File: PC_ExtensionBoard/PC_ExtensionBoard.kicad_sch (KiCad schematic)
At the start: 0 parts

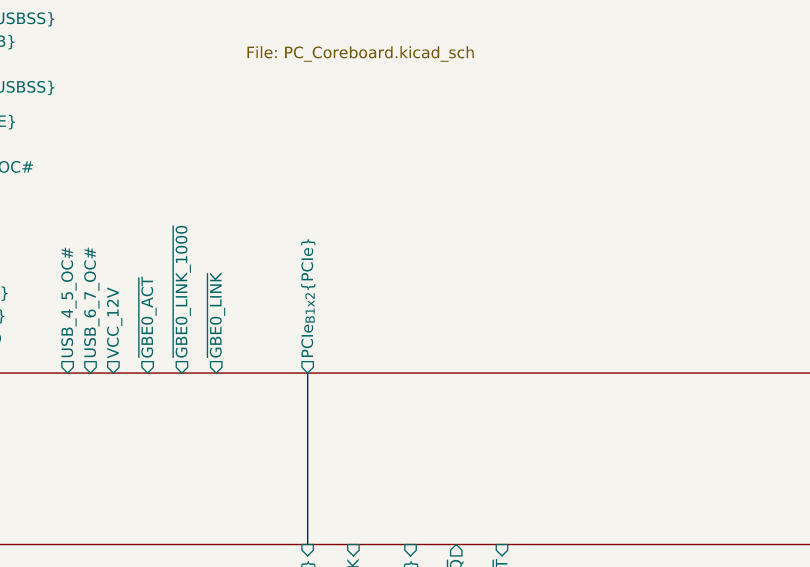
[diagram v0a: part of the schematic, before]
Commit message: update LCSC
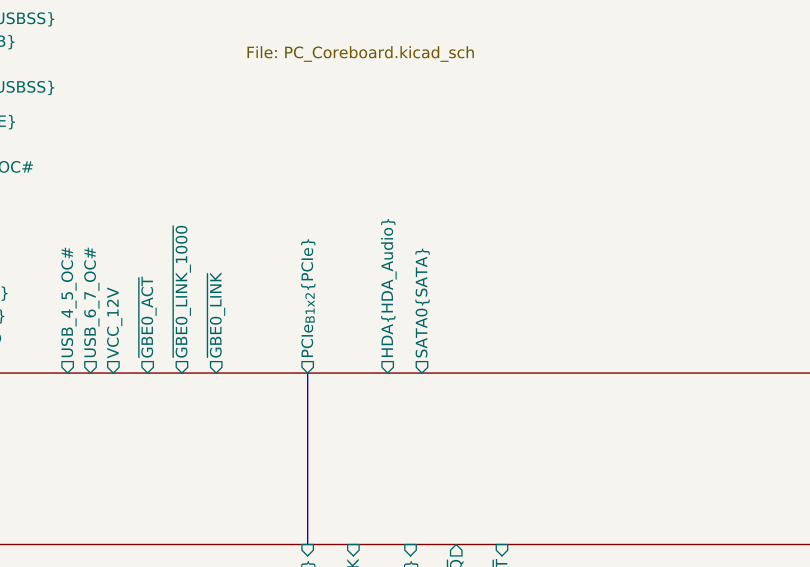
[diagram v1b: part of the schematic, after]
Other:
- sheet PC_CoreBoard ports: added HDA{HDA_Audio}, SATA0{SATA}; removed none
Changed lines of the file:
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@@
+			)
+		)
+		(pin "HDA{HDA_Audio}" output
+			(at 257.81 314.96 270)
+			(effects
+				(font
+					(size 1.27 1.27)
+				)
+				(justify left)
+			)
+		)
+		(pin "SATA0{SATA}" output
+			(at 261.62 314.96 270)
+			(effects
+				(font
+					(size 1.27 1.27)
+				)
+				(justify left)
 			)
 		)

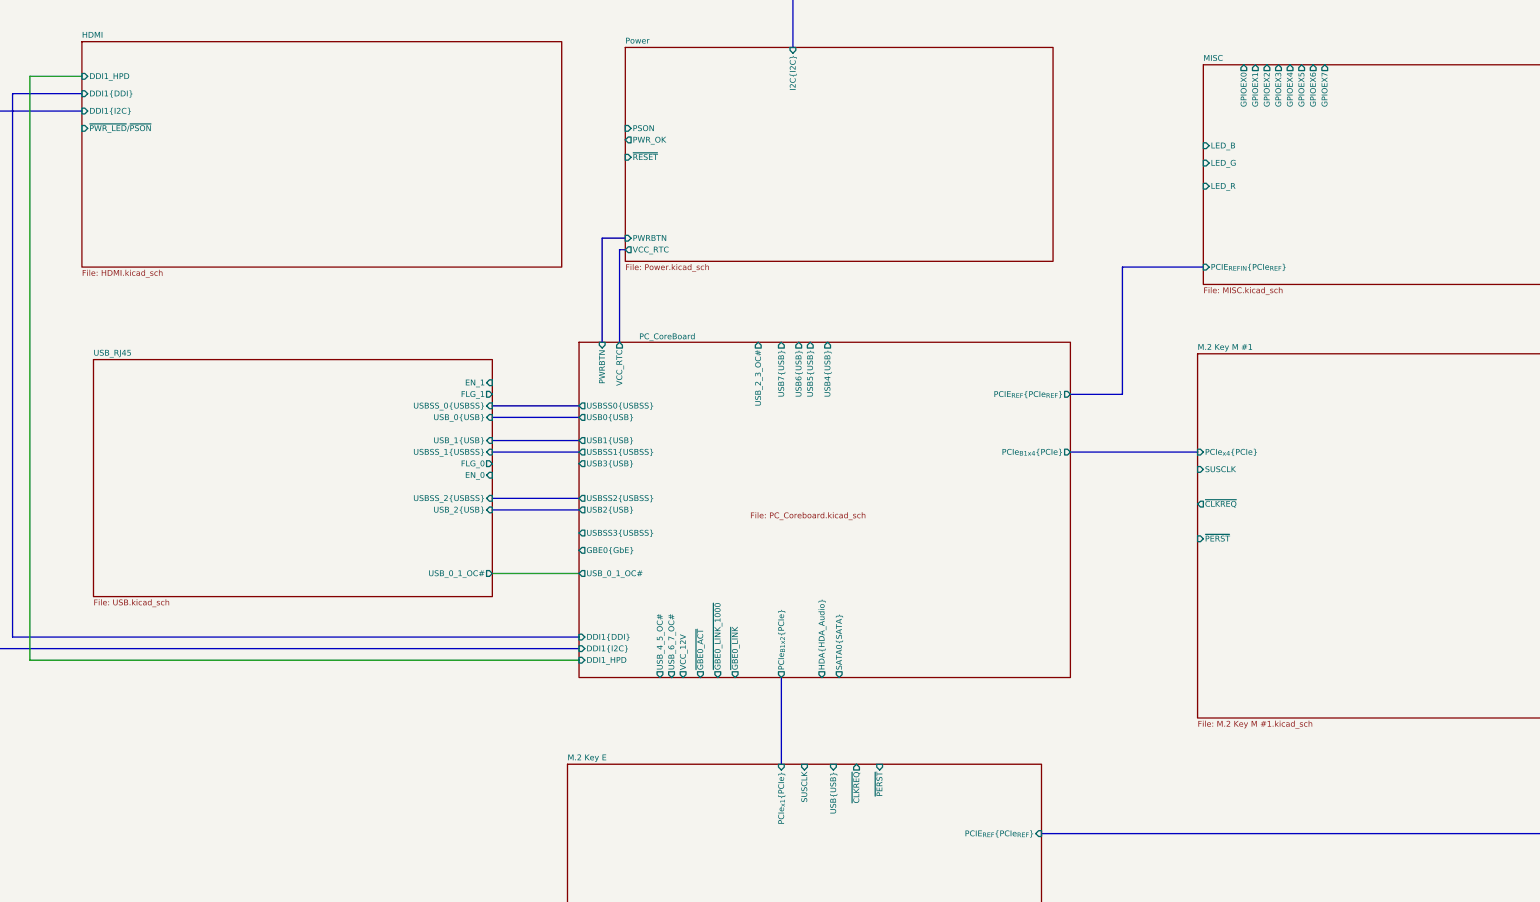
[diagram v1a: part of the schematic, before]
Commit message: update schematic
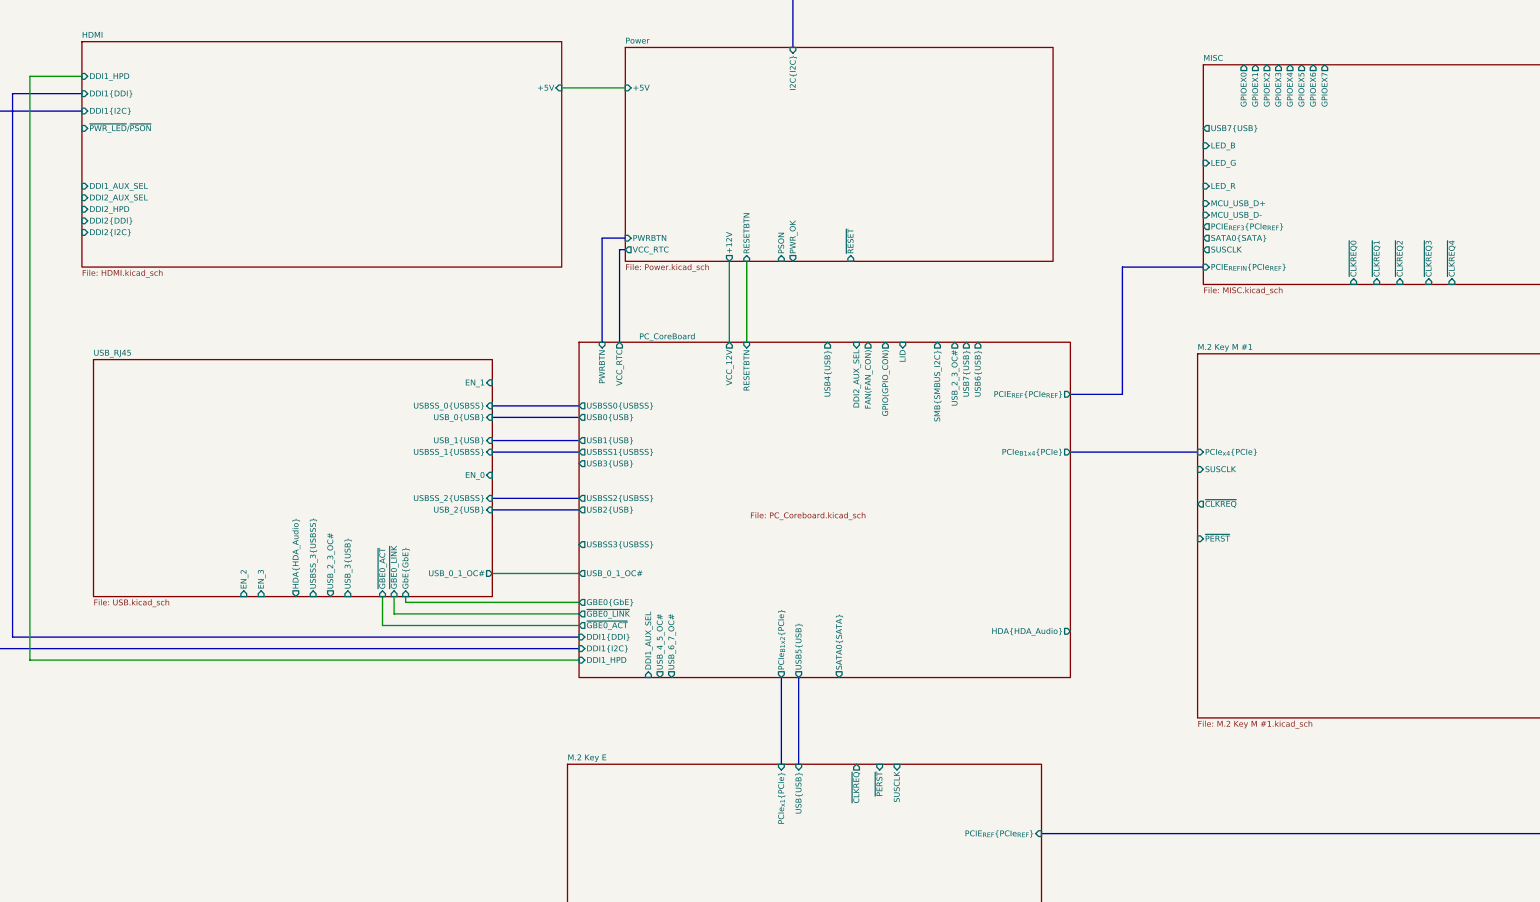
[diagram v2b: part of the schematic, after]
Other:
- sheet HDMI ports: added +5V, DDI1_AUX_SEL, DDI2_AUX_SEL, DDI2_HPD, DDI2{DDI}, DDI2{I2C}; removed none
- sheet MISC ports: added MCU_USB_D+, MCU_USB_D-, PCIE_{REF3}{PCIe_{REF}}, SATA0{SATA}, SUSCLK, USB7{USB}, ~{CLKREQ0}, ~{CLKREQ1}, ~{CLKREQ2}, ~{CLKREQ3}, ~{CLKREQ4}; removed none
- sheet PC_CoreBoard ports: added DDI1_AUX_SEL, DDI2_AUX_SEL, FAN(FAN_CON), GPIO(GPIO_CON), LID, RESETBTN, SMB{SMBUS_I2C}; removed ~{GBE0_LINK_1000}
- sheet Power ports: added +12V, +5V, RESETBTN; removed none
- sheet USB_RJ45 ports: added EN_2, EN_3, GbE{GbE}, HDA{HDA_Audio}, USBSS_3{USBSS}, USB_2_3_OC#, USB_3{USB}, ~{GBE0_ACT}, ~{GBE0_LINK}; removed FLG_0, FLG_1

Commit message: update LCSC Number
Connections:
- no-connect marks 0 -> 14
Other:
- sheet MISC ports: added EN0, EN1, EN2, EN3, FAN{FAN_CON}; removed MCU_USB_D+, MCU_USB_D-, PCIE_{REF1}{PCIe_{REF}}
- sheet PC_CoreBoard ports: added DDI2_HPD, DDI2{DDI}, DDI2{I2C}, FAN{FAN_CON}, GPIO{GPIO_CON}; removed FAN(FAN_CON), GPIO(GPIO_CON)

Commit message: update Schematic
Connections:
- no-connect marks 14 -> 28
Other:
- sheet M.2 Key M #1 ports: added PCIE1-4_SATA_PCIE; removed none
- sheet MISC ports: added SATA0-1_SATA_PCIE; removed LED_B, LED_G, LED_R
- sheet PC_CoreBoard ports: added PCIE1-4_SATA_PCIE, PWR_OK, SATA0-1_SATA_PCIE; removed none
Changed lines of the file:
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@@
+	)
+	(no_connect
+		(at 255.27 223.52)
 	)
 	(no_connect
@@
 	)
 	(no_connect
+		(at 95.25 196.85)
+	)
+	(no_connect
+		(at 264.16 241.3)
+	)
+	(no_connect
+		(at 222.25 322.58)
+	)
+	(no_connect
 		(at 383.54 228.6)
 	)
@@
 	)
 	(no_connect
+		(at 261.62 241.3)
+	)
+	(no_connect
+		(at 266.7 241.3)
+	)
+	(no_connect
+		(at 251.46 241.3)
+	)
+	(no_connect
+		(at 270.51 334.01)
+	)
+	(no_connect
 		(at 355.6 180.34)
 	)
 	(no_connect
+		(at 224.79 322.58)
+	)
+	(no_connect
+		(at 265.43 334.01)
+	)
+	(no_connect
+		(at 340.36 284.48)
+	)
+	(no_connect
 		(at 438.15 187.96)
 	)
@@
 	)
 	(no_connect
+		(at 251.46 223.52)
+	)
+	(no_connect
 		(at 358.14 180.34)
 	)
 	(no_connect
+		(at 259.08 241.3)
+	)
+	(no_connect
 		(at 368.3 180.34)
 	)
 	(no_connect
+		(at 340.36 276.86)
+	)
+	(no_connect
 		(at 375.92 228.6)
 	)
@@
 		)
 	)
+	(wire
+		(pts
+			(xy 295.91 227.33) (xy 295.91 241.3)
+		)
+		(stroke
+			(width 0)
+			(type default)
+		)
+	)
 	(bus
 		(pts
@@
 		)
 	)
+	(wire
+		(pts
+			(xy 295.91 227.33) (xy 316.23 227.33)
+		)
+		(stroke
+			(width 0)
+			(type default)
+		)
+	)
 	(bus
 		(pts
@@
 	(bus
 		(pts
-			(xy 226.06 241.3) (xy 226.06 223.52)
+			(xy 312.42 261.62) (xy 326.39 261.62)
 		)
 		(stroke
@@
 		)
 	)
+	(wire
+		(pts
+			(xy 226.06 223.52) (xy 226.06 241.3)
+		)
+		(stroke
+			(width 0)
+			(type default)
+		)
+	)
 	(bus
 		(pts
@@
 	(bus
 		(pts
-			(xy 228.6 241.3) (xy 228.6 223.52)
+			(xy 326.39 237.49) (xy 372.11 237.49)
 		)
 		(stroke
@@
 		)
 	)
+	(wire
+		(pts
+			(xy 341.63 217.17) (xy 316.23 217.17)
+		)
+		(stroke
+			(width 0)
+			(type default)
+		)
+	)
 	(bus
 		(pts
@@
 		)
 	)
+	(wire
+		(pts
+			(xy 316.23 217.17) (xy 316.23 227.33)
+		)
+		(stroke
+			(width 0)
+			(type default)
+		)
+	)
 	(bus
 		(pts
@@
 	(wire
 		(pts
+			(xy 228.6 223.52) (xy 228.6 241.3)
+		)
+		(stroke
+			(width 0)
+			(type default)
+		)
+	)
+	(wire
+		(pts
 			(xy 97.79 257.81) (xy 48.26 257.81)
 		)
@@
 		)
 	)
+	(bus
+		(pts
+			(xy 326.39 261.62) (xy 326.39 237.49)
+		)
+		(stroke
+			(width 0)
+			(type default)
+		)
+	)
 	(wire
 		(pts
@@
 	(wire
 		(pts
+			(xy 246.38 223.52) (xy 246.38 241.3)
+		)
+		(stroke
+			(width 0)
+			(type default)
+		)
+	)
+	(wire
+		(pts
 			(xy 378.46 143.51) (xy 378.46 180.34)
 		)
@@
 	(bus
 		(pts
+			(xy 372.11 237.49) (xy 372.11 228.6)
+		)
+		(stroke
+			(width 0)
+			(type default)
+		)
+	)
+	(bus
+		(pts
 			(xy 185.42 283.21) (xy 204.47 283.21)
+		)
+		(stroke
+			(width 0)
+			(type default)
+		)
+	)
+	(wire
+		(pts
+			(xy 312.42 292.1) (xy 340.36 292.1)
 		)
 		(stroke
@@
 		)
 		(pin "~{PWR_LED}{slash}~{PSON}" input
-			(at 95.25 199.39 180)
+			(at 95.25 196.85 180)
 			(effects
 				(font
@@
 		)
 		(pin "USB6{USB}" output
-			(at 292.1 241.3 90)
+			(at 266.7 241.3 90)
 			(effects
 				(font
@@
 		)
 		(pin "SATA0{SATA}" output
-			(at 261.62 322.58 270)
-			(effects
-				(font
-					(size 1.27 1.27)
-				)
-				(justify left)
+			(at 312.42 261.62 0)
+			(effects
+				(font
+					(size 1.27 1.27)
+				)
+				(justify right)
 			)
 		)
@@
 		)
 		(pin "LID" input
-			(at 275.59 241.3 90)
+			(at 251.46 241.3 90)
 			(effects
 				(font
@@
 		)
 		(pin "SMB{SMBUS_I2C}" output
-			(at 283.21 241.3 90)
+			(at 264.16 241.3 90)
 			(effects
 				(font
@@
 		)
 		(pin "GPIO{GPIO_CON}" output
-			(at 267.97 241.3 90)
+			(at 261.62 241.3 90)
+			(effects
+				(font
+					(size 1.27 1.27)
+				)
+				(justify right)
+			)
+		)
+		(pin "PWR_OK" input
+			(at 246.38 241.3 90)
+			(effects
+				(font
+					(size 1.27 1.27)
+				)
+				(justify right)
+			)
+		)
+		(pin "PCIE1-4_SATA_PCIE" input
+			(at 312.42 292.1 0)
+			(effects
+				(font
+					(size 1.27 1.27)
+				)
+				(justify right)
+			)
+		)
+		(pin "SATA0-1_SATA_PCIE" input
+			(at 295.91 241.3 90)
 			(effects
 				(font
@@
 			)
 		)
-		(pin "LED_B" input
-			(at 341.63 199.39 180)
-			(effects
-				(font
-					(size 1.27 1.27)
-				)
-				(justify left)
-			)
-		)
-		(pin "LED_G" input
-			(at 341.63 201.93 180)
-			(effects
-				(font
-					(size 1.27 1.27)
-				)
-				(justify left)
-			)
-		)
-		(pin "LED_R" input
-			(at 341.63 204.47 180)
-			(effects
-				(font
-					(size 1.27 1.27)
-				)
-				(justify left)
-			)
-		)
 		(pin "PCIE_{REF0}{PCIe_{REF}}" output
 			(at 438.15 217.17 0)
@@
 		)
 		(pin "SATA0{SATA}" output
-			(at 341.63 215.9 180)
+			(at 372.11 228.6 270)
 			(effects
 				(font
@@
 		(pin "FAN{FAN_CON}" output
 			(at 341.63 219.71 180)
+			(effects
+				(font
+					(size 1.27 1.27)
+				)
+				(justify left)
+			)
+		)
+		(pin "SATA0-1_SATA_PCIE" input
+			(at 341.63 217.17 180)
 			(effects
 				(font
@@
 		)
 		(pin "PSON" input
-			(at 248.92 223.52 270)
+			(at 251.46 223.52 270)
 			(effects
 				(font
@@
 		)
 		(pin "PWR_OK" output
-			(at 251.46 223.52 270)
+			(at 246.38 223.52 270)
 			(effects
 				(font
@@
 		)
 		(pin "~{RESET}" input
-			(at 264.16 223.52 270)
+			(at 255.27 223.52 270)
 			(effects
 				(font
@@
 			(effects
 				(font
+					(size 1.27 1.27)
+				)
+				(justify left)
+			)
+		)
+		(pin "PCIE1-4_SATA_PCIE" output
+			(at 340.36 292.1 180)
+			(effects
+				(font

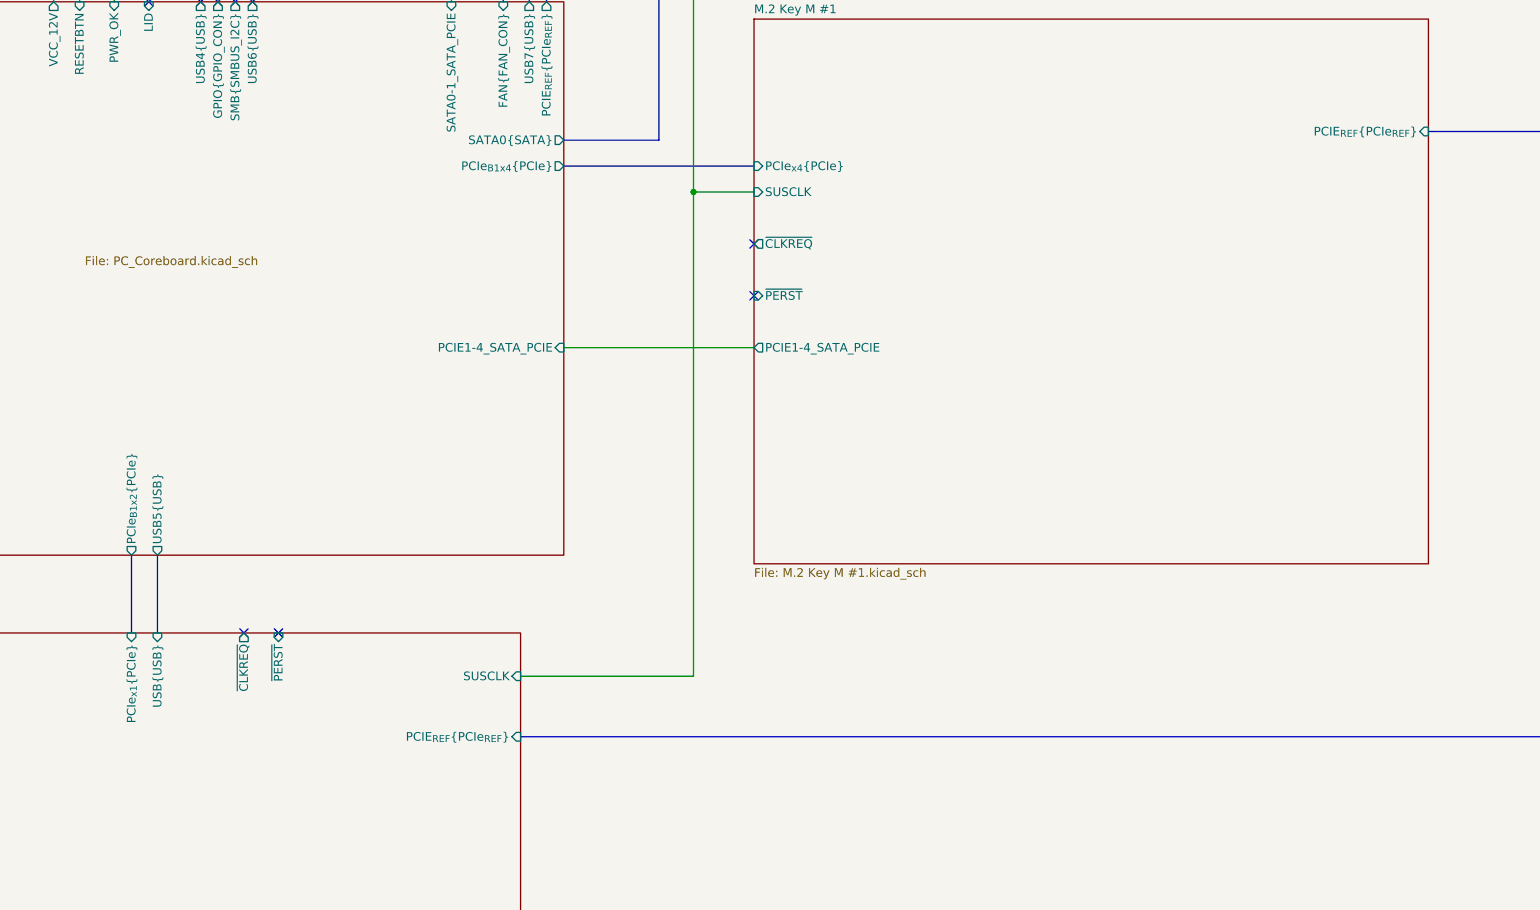
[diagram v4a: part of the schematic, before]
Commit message: attempts with impedance control
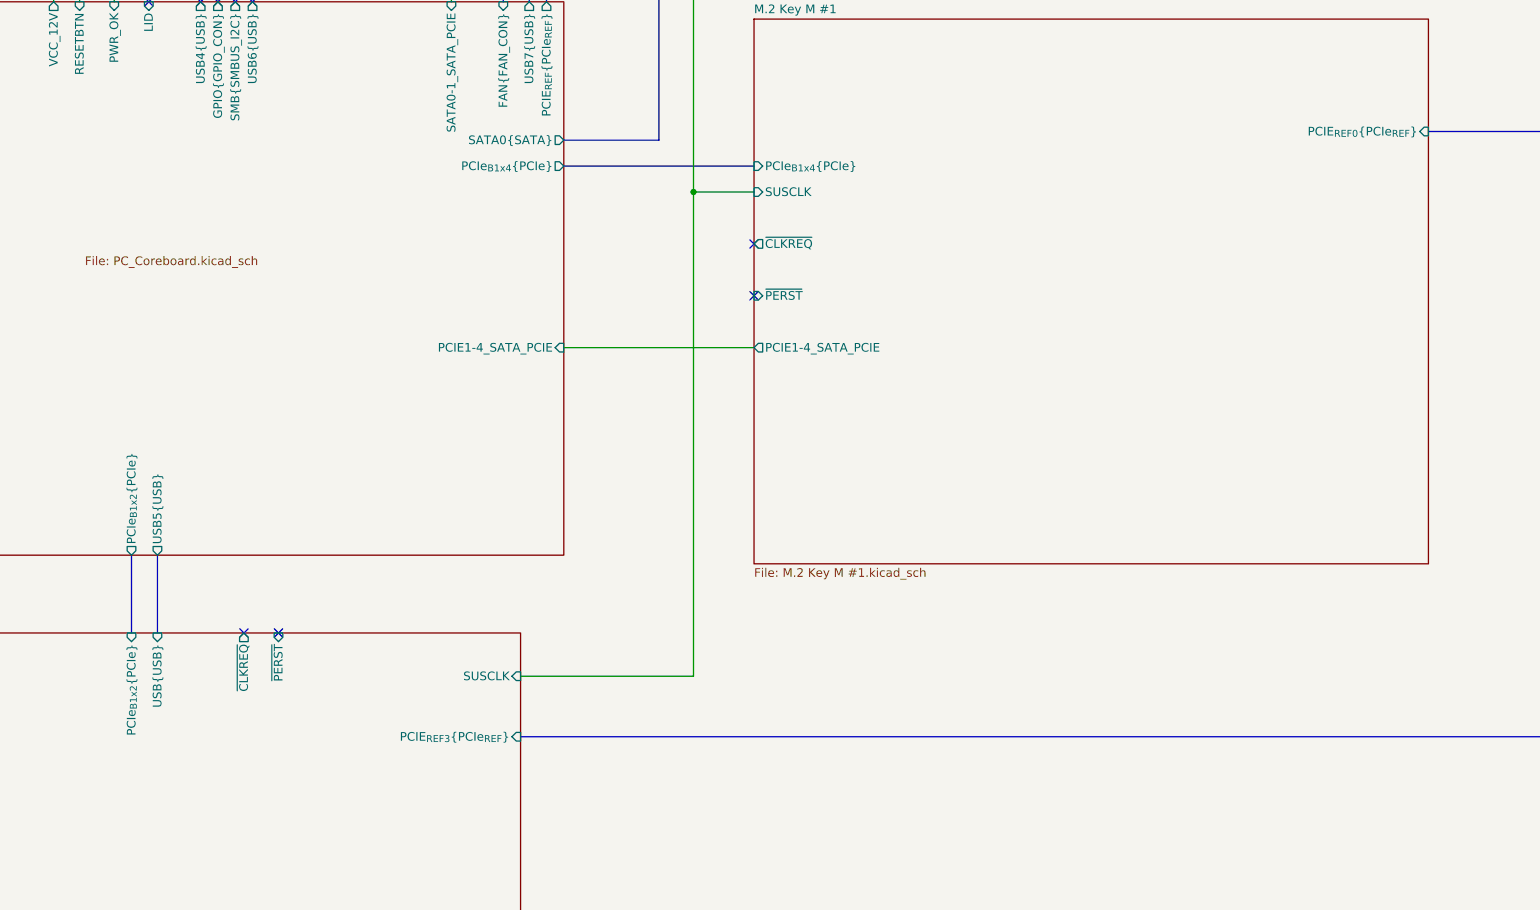
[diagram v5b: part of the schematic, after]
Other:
- sheet M.2 Key E ports: added PCIE_{REF3}{PCIe_{REF}}, PCIe_{B1x2}{PCIe}; removed PCIE_{REF}{PCIe_{REF}}, PCIe_{x1}{PCIe}
- sheet M.2 Key M #1 ports: added PCIE_{REF0}{PCIe_{REF}}, PCIe_{B1x4}{PCIe}; removed PCIE_{REF}{PCIe_{REF}}, PCIe_{x4}{PCIe}
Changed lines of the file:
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@@
-			)
-		)
-		(pin "PCIE_{REF}{PCIe_{REF}}" input
-			(at 306.07 349.25 0)
-			(effects
-				(font
-					(size 1.27 1.27)
-				)
-				(justify right)
-			)
-		)
-		(pin "PCIe_{x1}{PCIe}" input
-			(at 248.92 334.01 90)
-			(effects
-				(font
-					(size 1.27 1.27)
-				)
-				(justify right)
 			)
 		)
@@
 		(pin "~{PERST}" input
 			(at 270.51 334.01 90)
+			(effects
+				(font
+					(size 1.27 1.27)
+				)
+				(justify right)
+			)
+		)
+		(pin "PCIe_{B1x2}{PCIe}" input
+			(at 248.92 334.01 90)
+			(effects
+				(font
+					(size 1.27 1.27)
+				)
+				(justify right)
+			)
+		)
+		(pin "PCIE_{REF3}{PCIe_{REF}}" input
+			(at 306.07 349.25 0)
 			(effects
 				(font
@@
 			)
 		)
-		(pin "PCIE_{REF}{PCIe_{REF}}" input
-			(at 439.42 260.35 0)
-			(effects
-				(font
-					(size 1.27 1.27)
-				)
-				(justify right)
-			)
-		)
-		(pin "PCIe_{x4}{PCIe}" input
-			(at 340.36 265.43 180)
-			(effects
-				(font
-					(size 1.27 1.27)
-				)
-				(justify left)
-			)
-		)
 		(pin "SUSCLK" input
 			(at 340.36 269.24 180)
@@
 			)
 		)
+		(pin "PCIe_{B1x4}{PCIe}" input
+			(at 340.36 265.43 180)
+			(effects
+				(font
+					(size 1.27 1.27)
+				)
+				(justify left)
+			)
+		)
+		(pin "PCIE_{REF0}{PCIe_{REF}}" input
+			(at 439.42 260.35 0)
+			(effects
+				(font
+					(size 1.27 1.27)
+				)
+				(justify right)
+			)
+		)
